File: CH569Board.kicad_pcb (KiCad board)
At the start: 4 copper layers, 47.3 x 49.6 mm, 39 parts, among them CN1 BA42-80BT-1-NHB, J1 Conn_01x02_Male, J2 Conn_01x03_Male, U1 AMS1117-3.3, U2 AMS1117-1.2, U3 W25Q32JVSSIQ, U4 CH569W, X1 O705030MEEA4SC

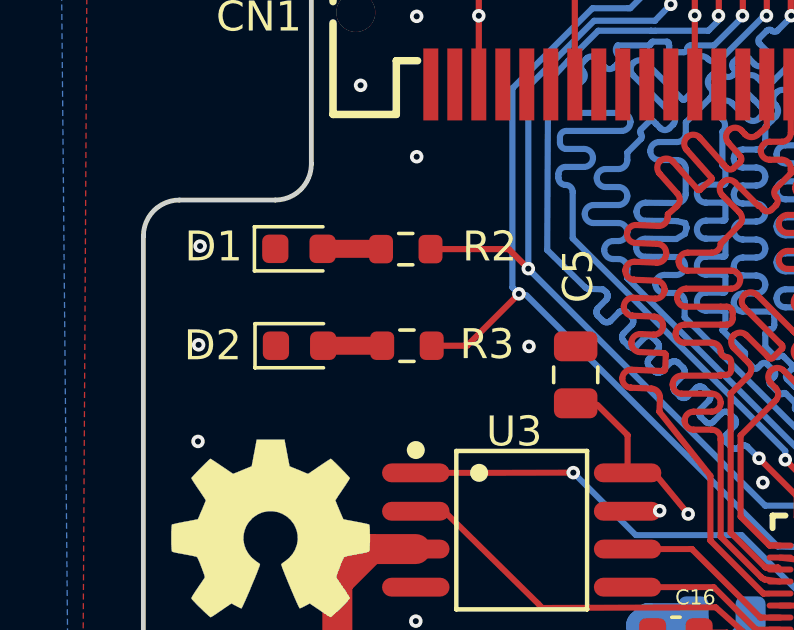
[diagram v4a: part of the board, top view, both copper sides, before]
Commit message: move LEDs to a better place
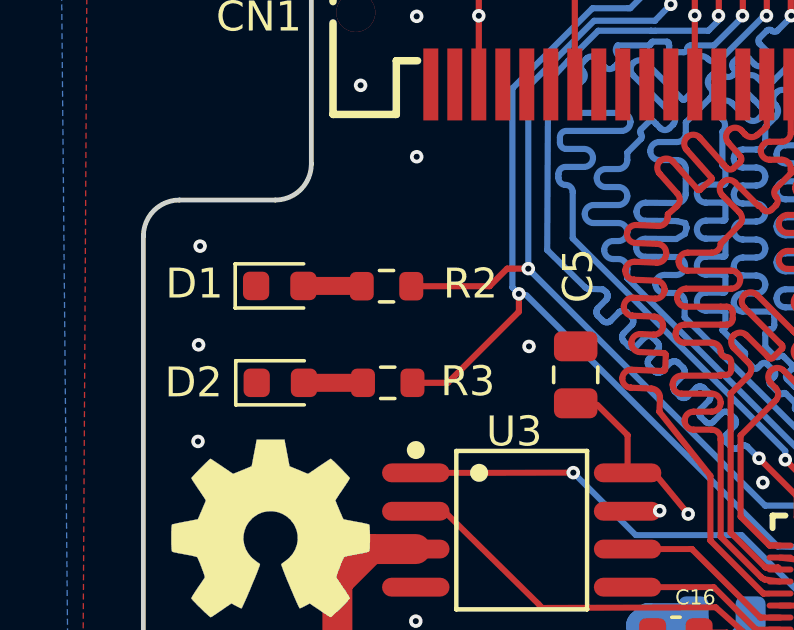
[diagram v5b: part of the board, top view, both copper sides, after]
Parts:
- moved D1 1.39 mm to (105.0, 91.5)
- moved D2 1.39 mm to (105.0, 94.7)
- moved R2 1.39 mm to (108.5, 91.5)
- moved R3 1.39 mm to (108.6, 94.7)
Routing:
- net /LED2: track 32.4 -> 33.9 mm
- net /LED1: track 32.2 -> 32.8 mm
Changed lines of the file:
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@@
   )
   (footprint "LED_SMD:LED_0603_1608Metric" (layer "F.Cu")
-    (at 105.635 93.5)
+    (at 104.9942 94.7362)
     (descr "LED SMD 0603 (1608 Metric), square (rectangular) end terminal, IPC_7351 nominal, (Body size source: http://www.tortai-tech.com/upload/download/2011102023233369053.pdf), generated with kicad-footprint-generator")
     (tags "LED")
@@
   )
   (footprint "LED_SMD:LED_0603_1608Metric" (layer "F.Cu")
-    (at 105.615 90.27)
+    (at 104.9742 91.5062)
     (descr "LED SMD 0603 (1608 Metric), square (rectangular) end terminal, IPC_7351 nominal, (Body size source: http://www.tortai-tech.com/upload/download/2011102023233369053.pdf), generated with kicad-footprint-generator")
     (tags "LED")
@@
   )
   (footprint "Resistor_SMD:R_0603_1608Metric" (layer "F.Cu")
-    (at 109.215 93.5)
+    (at 108.5742 94.7362)
     (descr "Resistor SMD 0603 (1608 Metric), square (rectangular) end terminal, IPC_7351 nominal, (Body size source: IPC-SM-782 page 72, https://www.pcb-3d.com/wordpress/wp-content/uploads/ipc-sm-782a_amendment_1_and_2.pdf), generated with kicad-footprint-generator")
     (tags "resistor")
@@
   )
   (footprint "Resistor_SMD:R_0603_1608Metric" (layer "F.Cu")
-    (at 109.175 90.28)
+    (at 108.5342 91.5162)
     (descr "Resistor SMD 0603 (1608 Metric), square (rectangular) end terminal, IPC_7351 nominal, (Body size source: IPC-SM-782 page 72, https://www.pcb-3d.com/wordpress/wp-content/uploads/ipc-sm-782a_amendment_1_and_2.pdf), generated with kicad-footprint-generator")
     (tags "resistor")
@@
   (segment (start 110.5304 123.2192) (end 113.6292 123.2192) (width 1) (layer "F.Cu") (net 23))
   (segment (start 113.68 123.27) (end 113.68 120.9964) (width 1) (layer "F.Cu") (net 23))
-  (segment (start 106.4025 90.27) (end 108.34 90.27) (width 0.6) (layer "F.Cu") (net 25))
-  (segment (start 108.34 90.27) (end 108.35 90.28) (width 0.6) (layer "F.Cu") (net 25))
+  (segment (start 105.7617 91.5062) (end 107.6992 91.5062) (width 0.6) (layer "F.Cu") (net 25))
   (segment (start 122.376995 104.562) (end 120.033 104.562) (width 0.2) (layer "F.Cu") (net 26))
   (segment (start 125.603 106.757) (end 125.603 107.312) (width 0.2) (layer "F.Cu") (net 26))
@@
   (arc (start 118.176946 91.743078) (mid 118.388313 91.832772) (end 118.474348 92.045652) (width 0.20574) (layer "B.Cu") (net 64))
   (arc (start 116.867122 89.031684) (mid 116.953159 89.244565) (end 117.164525 89.334259) (width 0.20574) (layer "B.Cu") (net 64))
-  (segment (start 110 90.28) (end 112.61 90.28) (width 0.20574) (layer "F.Cu") (net 65))
+  (segment (start 109.3592 91.5162) (end 111.9692 91.5162) (width 0.20574) (layer "F.Cu") (net 65))
+  (segment (start 112.5554 90.93) (end 111.9692 91.5162) (width 0.20574) (layer "F.Cu") (net 65))
   (segment (start 124.0026 99.41) (end 124.0026 98.841563) (width 0.20574) (layer "F.Cu") (net 65))
   (segment (start 124.0026 98.841563) (end 123.991255 98.830218) (width 0.20574) (layer "F.Cu") (net 65))
+  (segment (start 113.26 90.93) (end 112.5554 90.93) (width 0.20574) (layer "F.Cu") (net 65))
   (segment (start 118.01 82.12) (end 118.01 79.99) (width 0.20574) (layer "F.Cu") (net 65))
-  (segment (start 112.61 90.28) (end 113.26 90.93) (width 0.20574) (layer "F.Cu") (net 65))
   (via (at 123.991255 98.830218) (size 0.45) (drill 0.2) (layers "F.Cu" "B.Cu") (net 65))
   (via (at 118.01 82.12) (size 0.45) (drill 0.2) (layers "F.Cu" "B.Cu") (net 65))
@@
   (arc (start 115.541093 87.91) (mid 115.628961 88.122132) (end 115.841093 88.21) (width 0.20574) (layer "B.Cu") (net 66))
   (segment (start 117.21 81.68) (end 117.22 81.69) (width 0.20574) (layer "F.Cu") (net 67))
-  (segment (start 111.216422 93.5) (end 110.04 93.5) (width 0.20574) (layer "F.Cu") (net 67))
+  (segment (start 110.575622 94.7362) (end 109.3992 94.7362) (width 0.20574) (layer "F.Cu") (net 67))
+  (segment (start 112.945711 91.770711) (end 112.945711 92.366111) (width 0.20574) (layer "F.Cu") (net 67))
   (segment (start 122.58 100.22) (end 123.01 100.21) (width 0.20574) (layer "F.Cu") (net 67))
   (segment (start 123.2026 100.0174) (end 123.2026 99.41) (width 0.20574) (layer "F.Cu") (net 67))
-  (segment (start 112.945711 91.770711) (end 111.216422 93.5) (width 0.20574) (layer "F.Cu") (net 67))
+  (segment (start 112.945711 92.366111) (end 110.575622 94.7362) (width 0.20574) (layer "F.Cu") (net 67))
   (segment (start 117.21 79.99) (end 117.21 81.68) (width 0.20574) (layer "F.Cu") (net 67))
   (segment (start 123.01 100.21) (end 123.2026 100.0174) (width 0.20574) (layer "F.Cu") (net 67))
@@
   (segment (start 121.16937 105.39563) (end 120.429086 105.39563) (width 0.20574) (layer "F.Cu") (net 88))
   (segment (start 120.429086 105.39563) (end 119.717486 106.10723) (width 0.20574) (layer "F.Cu") (net 88))
-  (segment (start 106.4225 93.5) (end 108.39 93.5) (width 0.6) (layer "F.Cu") (net 90))
+  (segment (start 105.7817 94.7362) (end 107.7492 94.7362) (width 0.6) (layer "F.Cu") (net 90))
   (segment (start 117.7316 106.7308) (end 117.3988 106.4514) (width 0.20574) (layer "F.Cu") (net 94))
   (segment (start 117.3988 106.4514) (end 116.07 106.4514) (width 0.20574) (layer "F.Cu") (net 94))
